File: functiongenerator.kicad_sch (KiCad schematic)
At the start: 47 parts, among them J1 Amplitude, J2 offset, J3 Amplitude, J4 offset, J5 Conn_01x02_Socket, U1 LM6172, U2 LM6172, X1 ?2271611-, X2 ?2271611-

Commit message: pre release v2
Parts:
- added TP1, TP2, TP3, TP4, TP5, TP6: TestPoint_Small, TestPoint:TestPoint_Pad_D1.0mm, symbol Connector:TestPoint_Small
- C1, C3, C5: footprint functiongenerator:E2,5-7 -> Capacitor_THT:CP_Radial_D12.5mm_P5.00mm
- C2, C4, C6, C7, C8, C9: footprint functiongenerator:C025-030X050 -> Capacitor_THT:C_Disc_D3.0mm_W1.6mm_P2.50mm
- DC1: footprint functiongenerator:SIP3 -> Converter_DCDC:Converter_DCDC_TRACO_TSR-1_THT; symbol functiongenerator-eagle-import:R-78C-1.0 -> TSR_1-2450:TSR_1-2450; Availability (none) -> In Stock; Check_prices (none) -> https://www.snapeda.com/parts/TSR%201-2450/Traco+Power/view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; Description_1 (none) -> 1 Amp POL switching regulator, wide input range, pos.-pos. 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; MANUFACTURER (none) -> Traco Power; MAXIMUM_PACKAGE_HEIGHT (none) -> 10.6mm; MF (none) -> Traco Power; MP (none) -> TSR 1-2450; PARTREV (none) -> Apr 27, 2020; Package (none) -> SIP-3 Traco Power; Price (none) -> None; STANDARD (none) -> Manufacturer Recommendations; SnapEDA_Link (none) -> https://www.snapeda.com/parts/TSR%201-2450/Traco+Power/view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
- J5: footprint Connector_PinHeader_2.54mm:PinHeader_1x02_P2.54mm_Vertical -> Connector_PinSocket_2.54mm:PinSocket_1x02_P2.54mm_Vertical
- SV1: renamed from SV2; footprint functiongenerator:FE07 -> Connector_PinSocket_2.54mm:PinSocket_1x07_P2.54mm_Vertical
- SV2: renamed from SV1; footprint functiongenerator:FE07 -> Connector_PinSocket_2.54mm:PinSocket_1x07_P2.54mm_Vertical
- SV4: footprint Connector_PinHeader_2.54mm:PinHeader_1x04_P2.54mm_Vertical -> Connector_PinSocket_2.54mm:PinSocket_1x04_P2.54mm_Vertical
- X1, X2: footprint functiongenerator:AMP_227161 -> Connector_Coaxial:LEMO-EPL.00.250.NTN
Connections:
- net at J3.1 (Pin_1), R6.2, U2.1: now also TP5.1
- net at R8.1, U2.7, X2.1: now also TP6.1
- net at R4.1, U1.7, X1.1: now also TP3.1
- net at J1.1 (Pin_1), R1.2, U1.1: now also TP2.1
- net at R13.1, SV2.1: now also TP4.1
- net at R10.1, SV1.1: now also TP1.1
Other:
- moved on the sheet: C3, D1, R9

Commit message: optimized pcb layout
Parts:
- C1: value ~ -> 470uF; symbol functiongenerator-eagle-import:CPOL-EUE2.5-7 -> Device:C_Polarized
- C10: renamed from C2; symbol functiongenerator-eagle-import:C-EU025-030X050 -> Device:C_Small
- C13: renamed from C6; symbol functiongenerator-eagle-import:C-EU025-030X050 -> Device:C_Small
- C14: renamed from C7; symbol functiongenerator-eagle-import:C-EU025-030X050 -> Device:C_Small
- C17: renamed from C3; value ~ -> 10uF; symbol functiongenerator-eagle-import:CPOL-EUE2.5-7 -> Device:C_Polarized
- C2: renamed from C5; value ~ -> 470uF; symbol functiongenerator-eagle-import:CPOL-EUE2.5-7 -> Device:C_Polarized
- C4: renamed from C8; symbol functiongenerator-eagle-import:C-EU025-030X050 -> Device:C_Small
- C5: renamed from C9; symbol functiongenerator-eagle-import:C-EU025-030X050 -> Device:C_Small
- C7: renamed from C16; value 2.2uF -> 10uF
- C8: renamed from C17; value 2.2uF -> 10uF
- C9: renamed from C4; symbol functiongenerator-eagle-import:C-EU025-030X050 -> Device:C_Small
- R1: renamed from R2; value 33 -> 330; footprint functiongenerator:0204_7 -> Resistor_THT:R_Axial_DIN0204_L3.6mm_D1.6mm_P7.62mm_Horizontal; symbol functiongenerator-eagle-import:R-EU_0204/7 -> Device:R
- R10: renamed from R4; footprint functiongenerator:0204_7 -> Resistor_THT:R_Axial_DIN0204_L3.6mm_D1.6mm_P7.62mm_Horizontal; symbol functiongenerator-eagle-import:R-EU_0204/7 -> Device:R
- R11: renamed from R7; footprint functiongenerator:0204_7 -> Resistor_THT:R_Axial_DIN0204_L3.6mm_D1.6mm_P7.62mm_Horizontal; symbol functiongenerator-eagle-import:R-EU_0204/7 -> Device:R
- R12: renamed from R8; footprint functiongenerator:0204_7 -> Resistor_THT:R_Axial_DIN0204_L3.6mm_D1.6mm_P7.62mm_Horizontal; symbol functiongenerator-eagle-import:R-EU_0204/7 -> Device:R
- R2: renamed from R3; value 33 -> 330; footprint functiongenerator:0204_7 -> Resistor_THT:R_Axial_DIN0204_L3.6mm_D1.6mm_P7.62mm_Horizontal; symbol functiongenerator-eagle-import:R-EU_0204/7 -> Device:R
- R7: renamed from R1; footprint functiongenerator:0204_7 -> Resistor_THT:R_Axial_DIN0204_L3.6mm_D1.6mm_P7.62mm_Horizontal; symbol functiongenerator-eagle-import:R-EU_0204/7 -> Device:R
- R8: renamed from R6; footprint functiongenerator:0204_7 -> Resistor_THT:R_Axial_DIN0204_L3.6mm_D1.6mm_P7.62mm_Horizontal; symbol functiongenerator-eagle-import:R-EU_0204/7 -> Device:R_Small
- R9: renamed from R5; footprint functiongenerator:0204_7 -> Resistor_THT:R_Axial_DIN0204_L3.6mm_D1.6mm_P7.62mm_Horizontal; symbol functiongenerator-eagle-import:R-EU_0204/7 -> Device:R
- RV1: value R_Potentiometer_Trim -> 2k
- SV1: renamed from SV3; symbol functiongenerator-eagle-import:MA03-1 -> Connector:Screw_Terminal_01x03
- SV3: renamed from SV1; value FE07-1 -> Conn_01x07_Socket; symbol functiongenerator-eagle-import:FE07-1 -> Connector:Conn_01x07_Socket
- SV4: renamed from SV2; symbol functiongenerator-eagle-import:FE07-1 -> Connector:Conn_01x07_Socket
- X1: value ?2271611- -> CON1; footprint Connector_Coaxial:LEMO-EPL.00.250.NTN -> BNC:LINX_CONBNC002; symbol functiongenerator-eagle-import:?2271611- -> CONBNC002:CONBNC002; Availability (none) -> In Stock; Check_prices (none) -> https://www.snapeda.com/parts/CONBNC002/TE+Connectivity/vie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; Description_1 (none) -> BNC Jack 50 Ohm PCB Through Hole; MF (none) -> TE Connectivity; MP (none) -> CONBNC002; Package (none) -> None; Price (none) -> None; Purchase-URL (none) -> https://www.snapeda.com/api/url_track_click_mouser/?unipart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; SnapEDA_Link (none) -> https://www.snapeda.com/parts/CONBNC002/TE+Connectivity/vie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
- X2: value ?2271611- -> CON2; footprint Connector_Coaxial:LEMO-EPL.00.250.NTN -> BNC:LINX_CONBNC002; symbol functiongenerator-eagle-import:?2271611- -> CONBNC002:CONBNC002; Availability (none) -> In Stock; Check_prices (none) -> https://www.snapeda.com/parts/CONBNC002/TE+Connectivity/vie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; Description_1 (none) -> BNC Jack 50 Ohm PCB Through Hole; MF (none) -> TE Connectivity; MP (none) -> CONBNC002; Package (none) -> None; Price (none) -> None; Purchase-URL (none) -> https://www.snapeda.com/api/url_track_click_mouser/?unipart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; SnapEDA_Link (none) -> https://www.snapeda.com/parts/CONBNC002/TE+Connectivity/vie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
- renumbered C12 to C11, C13 to C12, C14 to C15, C15 to C16, C10 to C3, C11 to C6, J5 to J1, J1 to J2, J2 to J4, J4 to J5, R9 to R13, R11 to R3, R10 to R4, R12 to R5, R13 to R6, SV4 to SV2, TP4 to TP2, TP2 to TP3, TP5 to TP4, TP3 to TP5
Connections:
- net +12v: now also C1.1; no longer C1.+
- net +5v: now also C17.1; no longer C17.+
- net -12v: now also C2.2; no longer C2.+
- net GND: now also C1.2, C17.2, C2.1, X1.S1, X1.S2, X2.S1, X2.S2; no longer C1.-, C17.-, C2.-
- net at J3.1 (Pin_1), TP4.1, U2.1: now also R8.1; no longer R8.2
- net at R12.2, U2.6 (-): now also R8.2; no longer R8.1
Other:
- moved on the sheet: J2, J3, J4, J5

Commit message: optimizing pcb design
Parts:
- R1, R11, R2, R9: footprint Resistor_THT:R_Axial_DIN0204_L3.6mm_D1.6mm_P7.62mm_Horizontal -> Resistor_THT:R_Axial_DIN0207_L6.3mm_D2.5mm_P7.62mm_Horizontal
- R10, R12, R7, R8: value 1000 -> 1k; footprint Resistor_THT:R_Axial_DIN0204_L3.6mm_D1.6mm_P7.62mm_Horizontal -> Resistor_THT:R_Axial_DIN0207_L6.3mm_D2.5mm_P7.62mm_Horizontal
- R13: value 390 -> 330
- R3, R4, R5, R6: footprint Resistor_THT:R_Axial_DIN0204_L3.6mm_D1.6mm_P5.08mm_Horizontal -> Resistor_THT:R_Axial_DIN0207_L6.3mm_D2.5mm_P7.62mm_Horizontal
- RV2: value R_Potentiometer_Trim -> 2k
- SV1: footprint TerminalBlock_Phoenix:TerminalBlock_Phoenix_PT-1,5-3-3.5-H_1x03_P3.50mm_Horizontal -> TerminalBlock_MetzConnect:TerminalBlock_MetzConnect_Type059_RT06303HBWC_1x03_P3.50mm_Horizontal
- SV4: value FE07-1 -> Conn_01x07_Socket
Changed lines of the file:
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@@
 			)
 		)
-		(property "Value" "1000"
+		(property "Value" "1k"
 			(at 160.782 127.508 90)
 			(effects
@@
 			)
 		)
-		(property "Footprint" "Resistor_THT:R_Axial_DIN0204_L3.6mm_D1.6mm_P7.62mm_Horizontal"
+		(property "Footprint" "Resistor_THT:R_Axial_DIN0207_L6.3mm_D2.5mm_P7.62mm_Horizontal"
 			(at 163.83 129.54 0)
 			(effects
@@
 			)
 		)
-		(property "Value" "R_Potentiometer_Trim"
+		(property "Value" "2k"
 			(at 113.7921 158.6921 0)
 			(effects
@@
 			)
 		)
-		(property "Footprint" "Resistor_THT:R_Axial_DIN0204_L3.6mm_D1.6mm_P7.62mm_Horizontal"
+		(property "Footprint" "Resistor_THT:R_Axial_DIN0207_L6.3mm_D2.5mm_P7.62mm_Horizontal"
 			(at 163.83 154.94 0)
 			(effects
@@
 			)
 		)
-		(property "Footprint" "Resistor_THT:R_Axial_DIN0204_L3.6mm_D1.6mm_P5.08mm_Horizontal"
+		(property "Footprint" "Resistor_THT:R_Axial_DIN0207_L6.3mm_D2.5mm_P7.62mm_Horizontal"
 			(at 119.38 114.808 90)
 			(effects
@@
 			)
 		)
-		(property "Value" "FE07-1"
+		(property "Value" "Conn_01x07_Socket"
 			(at 92.71 135.89 0)
 			(effects
@@
 				)
 				(justify left bottom)
-				(hide yes)
 			)
 		)
@@
 			)
 		)
-		(property "Footprint" "Resistor_THT:R_Axial_DIN0204_L3.6mm_D1.6mm_P5.08mm_Horizontal"
+		(property "Footprint" "Resistor_THT:R_Axial_DIN0207_L6.3mm_D2.5mm_P7.62mm_Horizontal"
 			(at 124.46 164.338 90)
 			(effects
@@
 			)
 		)
-		(property "Footprint" "Resistor_THT:R_Axial_DIN0204_L3.6mm_D1.6mm_P5.08mm_Horizontal"
+		(property "Footprint" "Resistor_THT:R_Axial_DIN0207_L6.3mm_D2.5mm_P7.62mm_Horizontal"
 			(at 119.38 118.618 90)
 			(effects
@@
 			)
 		)
-		(property "Value" "390"
+		(property "Value" "330"
 			(at 189.484 75.438 90)
 			(effects
@@
 			)
 		)
-		(property "Value" "1000"
+		(property "Value" "1k"
 			(at 149.606 117.094 90)
 			(effects
@@
 			)
 		)
-		(property "Footprint" "Resistor_THT:R_Axial_DIN0204_L3.6mm_D1.6mm_P7.62mm_Horizontal"
+		(property "Footprint" "Resistor_THT:R_Axial_DIN0207_L6.3mm_D2.5mm_P7.62mm_Horizontal"
 			(at 152.4 119.38 0)
 			(effects
@@
 			)
 		)
-		(property "Footprint" "Resistor_THT:R_Axial_DIN0204_L3.6mm_D1.6mm_P5.08mm_Horizontal"
+		(property "Footprint" "Resistor_THT:R_Axial_DIN0207_L6.3mm_D2.5mm_P7.62mm_Horizontal"
 			(at 124.46 160.528 90)
 			(effects
@@
 			)
 		)
-		(property "Footprint" "Resistor_THT:R_Axial_DIN0204_L3.6mm_D1.6mm_P7.62mm_Horizontal"
+		(property "Footprint" "Resistor_THT:R_Axial_DIN0207_L6.3mm_D2.5mm_P7.62mm_Horizontal"
 			(at 158.75 109.22 0)
 			(effects
@@
 			)
 		)
-		(property "Value" "1000"
+		(property "Value" "1k"
 			(at 165.354 172.72 90)
 			(effects
@@
 			)
 		)
-		(property "Footprint" "Resistor_THT:R_Axial_DIN0204_L3.6mm_D1.6mm_P7.62mm_Horizontal"
+		(property "Footprint" "Resistor_THT:R_Axial_DIN0207_L6.3mm_D2.5mm_P7.62mm_Horizontal"
 			(at 167.64 175.26 0)
 			(effects
@@
 			)
 		)
-		(property "Value" "1000"
+		(property "Value" "1k"
 			(at 160.02 167.132 90)
 			(effects
@@
 			)
 		)
-		(property "Footprint" "Resistor_THT:R_Axial_DIN0204_L3.6mm_D1.6mm_P7.62mm_Horizontal"
+		(property "Footprint" "Resistor_THT:R_Axial_DIN0207_L6.3mm_D2.5mm_P7.62mm_Horizontal"
 			(at 157.48 165.1 0)
 			(effects
@@
 			)
 		)
-		(property "Footprint" "TerminalBlock_Phoenix:TerminalBlock_Phoenix_PT-1,5-3-3.5-H_1x03_P3.50mm_Horizontal"
+		(property "Footprint" "TerminalBlock_MetzConnect:TerminalBlock_MetzConnect_Type059_RT06303HBWC_1x03_P3.50mm_Horizontal"
 			(at 76.2 71.12 0)
 			(effects
@@
 			)
 		)
-		(property "Footprint" "Resistor_THT:R_Axial_DIN0204_L3.6mm_D1.6mm_P7.62mm_Horizontal"
+		(property "Footprint" "Resistor_THT:R_Axial_DIN0207_L6.3mm_D2.5mm_P7.62mm_Horizontal"
 			(at 105.41 167.64 0)
 			(effects
@@
 			)
 		)
-		(property "Footprint" "Resistor_THT:R_Axial_DIN0204_L3.6mm_D1.6mm_P7.62mm_Horizontal"
+		(property "Footprint" "Resistor_THT:R_Axial_DIN0207_L6.3mm_D2.5mm_P7.62mm_Horizontal"
 			(at 102.87 129.54 0)
 			(effects

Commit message: optimizing pcb design
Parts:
- added R2, R4: 680, Resistor_THT:R_Axial_DIN0207_L6.3mm_D2.5mm_P7.62mm_Horizontal, symbol Device:R
- R11: renamed from R9; value 500 -> 520
- R13: renamed from R11; value 500 -> 520
- R5: renamed from R3; value 18k -> 10k
- R7: renamed from R5; value 18k -> 10k
- RV1, RV2: value 2k -> 500
- renumbered R8 to R10, R10 to R12, R12 to R14, R13 to R15, R2 to R3, R4 to R6, R6 to R8, R7 to R9
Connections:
- net -12v: now also R2.1, R4.1; no longer RV1.3, RV2.3
- new net: R4.2, RV2.3
- new net: R2.2, RV1.3
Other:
- moved on the sheet: RV1, RV2

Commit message: added gnd to inout connector to reduce grounding loops
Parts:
- SV2: value Conn_01x04_Socket -> Conn_01x05_Socket; footprint Connector_PinSocket_2.54mm:PinSocket_1x04_P2.54mm_Vertical -> Connector_PinSocket_2.54mm:PinSocket_1x05_P2.54mm_Vertical; symbol Connector:Conn_01x04_Socket -> Connector:Conn_01x05_Socket
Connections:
- net GND: now also SV2.5 (Pin_5)
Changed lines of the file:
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@@
+	(symbol
+		(lib_id "power:GND")
+		(at 81.28 109.22 90)
+		(unit 1)
+		(exclude_from_sim no)
+		(in_bom yes)
+		(on_board yes)
+		(dnp no)
+		(fields_autoplaced yes)
+		(property "Reference" "#PWR020"
+			(at 87.63 109.22 0)
+			(effects
+				(font
+					(size 1.27 1.27)
+				)
+				(hide yes)
+			)
+		)
+		(property "Value" "GND"
+			(at 84.455 109.22 90)
+			(effects
+				(font
+					(size 1.27 1.27)
+				)
+				(justify right)
+			)
+		)
+		(property "Footprint" ""
+			(at 81.28 109.22 0)
+			(effects
+				(font
+					(size 1.27 1.27)
+				)
+				(hide yes)
+			)
+		)
+		(property "Datasheet" ""
+			(at 81.28 109.22 0)
+			(effects
+				(font
+					(size 1.27 1.27)
+				)
+				(hide yes)
+			)
+		)
+		(property "Description" "Power symbol creates a global label with name \"GND\" , ground"
+			(at 81.28 109.22 0)
+			(effects
+				(font
+					(size 1.27 1.27)
+				)
+				(hide yes)
+			)
+		)
+		(pin "1"
+		)
+		(instances
+			(project "functiongenerator"
+				(path "/5565f228-82ce-48d9-9419-b221a0e0c70a"
+					(reference "#PWR020")
+					(unit 1)
+				)
+			)
+		)
+	)
 	(symbol
 		(lib_id "power:GND")
@@
 	)
 	(symbol
-		(lib_id "Connector:Conn_01x04_Socket")
-		(at 76.2 116.84 180)
+		(lib_id "Connector:Conn_01x05_Socket")
+		(at 76.2 114.3 180)
 		(unit 1)
 		(exclude_from_sim no)
@@
 		(dnp no)
 		(property "Reference" "SV2"
-			(at 78.994 120.904 0)
+			(at 78.994 118.364 0)
 			(effects
 				(font
@@
 			)
 		)
-		(property "Value" "Conn_01x04_Socket"
-			(at 76.2 109.22 0)
-			(effects
-				(font
-					(size 1.27 1.27)
-				)
-				(hide yes)
-			)
-		)
-		(property "Footprint" "Connector_PinSocket_2.54mm:PinSocket_1x04_P2.54mm_Vertical"
-			(at 76.2 116.84 0)
+		(property "Value" "Conn_01x05_Socket"
+			(at 76.2 106.68 0)
+			(effects
+				(font
+					(size 1.27 1.27)
+				)
+				(hide yes)
+			)
+		)
+		(property "Footprint" "Connector_PinSocket_2.54mm:PinSocket_1x05_P2.54mm_Vertical"
+			(at 76.2 114.3 0)
 			(effects
 				(font
@@
 		)
 		(property "Datasheet" "~"
-			(at 76.2 116.84 0)
+			(at 76.2 114.3 0)
 			(effects
 				(font
@@
 		)
 		(property "Description" "Generic connector, single row, 01x04, script generated"
-			(at 76.2 116.84 0)
+			(at 76.2 114.3 0)
 			(effects
 				(font
@@
 		(pin "4"
 		)
-		(instances
+		(pin "5"
+		)
+		(instances

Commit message: attached agnd to common gnd moved +5v connector to board edge
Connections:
- net GND: now also SV3.2 (Pin_2), SV4.2 (Pin_2)
- no-connect marks 2 -> 0
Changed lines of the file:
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@@
+	)
+	(junction
+		(at 96.52 143.51)
+		(diameter 0)
+		(color 0 0 0 0)
 	)
 	(junction
@@
 	)
 	(junction
+		(at 96.52 109.22)
+		(diameter 0)
+		(color 0 0 0 0)
+	)
+	(junction
 		(at 105.41 148.59)
 		(diameter 0)
@@
 		(color 0 0 0 0)
 	)
-	(no_connect
-		(at 96.52 153.67)
-	)
-	(no_connect
-		(at 96.52 119.38)
-	)
 	(wire
 		(pts
@@
 	(wire
 		(pts
+			(xy 96.52 119.38) (xy 99.06 119.38)
+		)
+		(stroke
+			(width 0)
+			(type default)
+		)
+	)
+	(wire
+		(pts
 			(xy 106.68 116.84) (xy 106.68 121.92)
 		)
@@
 	(wire
 		(pts
+			(xy 97.79 144.78) (xy 96.52 144.78)
+		)
+		(stroke
+			(width 0)
+			(type default)
+		)
+	)
+	(wire
+		(pts
 			(xy 105.41 140.97) (xy 105.41 143.51)
 		)
@@
 	(wire
 		(pts
+			(xy 96.52 110.49) (xy 99.06 110.49)
+		)
+		(stroke
+			(width 0)
+			(type default)
+		)
+	)
+	(wire
+		(pts
+			(xy 99.06 110.49) (xy 99.06 119.38)
+		)
+		(stroke
+			(width 0)
+			(type default)
+		)
+	)
+	(wire
+		(pts
 			(xy 115.57 109.22) (xy 115.57 113.03)
 		)
@@
 	(wire
 		(pts
+			(xy 96.52 153.67) (xy 97.79 153.67)
+		)
+		(stroke
+			(width 0)
+			(type default)
+		)
+	)
+	(wire
+		(pts
 			(xy 143.51 156.21) (xy 144.78 156.21)
 		)
@@
 	(wire
 		(pts
+			(xy 96.52 109.22) (xy 96.52 110.49)
+		)
+		(stroke
+			(width 0)
+			(type default)
+		)
+	)
+	(wire
+		(pts
 			(xy 105.41 99.06) (xy 105.41 101.6)
 		)
@@
 	(wire
 		(pts
+			(xy 96.52 143.51) (xy 96.52 144.78)
+		)
+		(stroke
+			(width 0)
+			(type default)
+		)
+	)
+	(wire
+		(pts
 			(xy 81.28 116.84) (xy 96.52 116.84)
 		)
@@
 		)
 		(stroke
+			(width 0)
+			(type default)
+		)
+	)
+	(wire
+		(pts
+			(xy 97.79 153.67) (xy 97.79 144.78)
+		)
+		(stroke

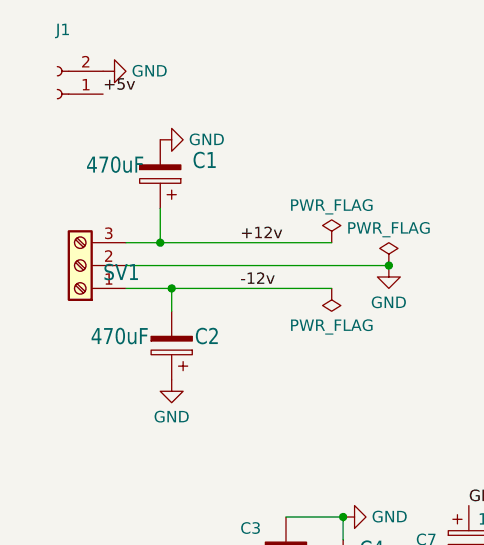
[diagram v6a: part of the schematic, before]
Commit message: seperated channels more updated label to v1.1
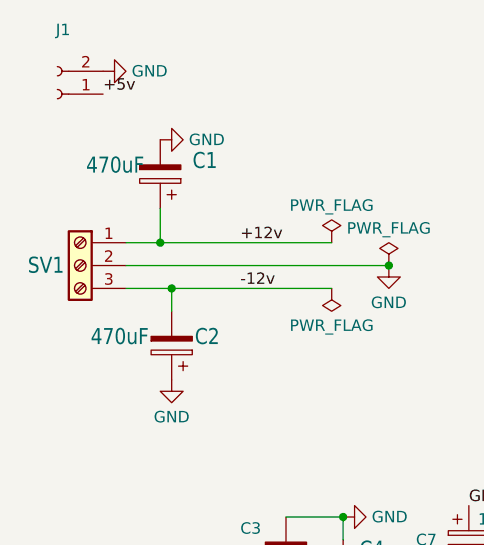
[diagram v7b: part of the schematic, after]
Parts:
- J2, J3: footprint Connector_JST:JST_XH_B2B-XH-AM_1x02_P2.50mm_Vertical -> Connector_JST:JST_XH_B2B-XH-A_1x02_P2.50mm_Vertical
- J4, J5: footprint Connector_JST:JST_XH_B3B-XH-AM_1x03_P2.50mm_Vertical -> Connector_JST:JST_XH_B3B-XH-A_1x03_P2.50mm_Vertical
- SV1: footprint TerminalBlock_MetzConnect:TerminalBlock_MetzConnect_Type059_RT06303HBWC_1x03_P3.50mm_Horizontal -> TerminalBlock_Phoenix:TerminalBlock_Phoenix_PT-1,5-3-3.5-H_1x03_P3.50mm_Horizontal
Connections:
- net +12v: now also SV1.1 (Pin_1); no longer SV1.3 (Pin_3)
- net -12v: now also SV1.3 (Pin_3); no longer SV1.1 (Pin_1)
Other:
- moved on the sheet: SV1
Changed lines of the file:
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@@
 			)
 		)
-		(property "Footprint" "Connector_JST:JST_XH_B2B-XH-AM_1x02_P2.50mm_Vertical"
+		(property "Footprint" "Connector_JST:JST_XH_B2B-XH-A_1x02_P2.50mm_Vertical"
 			(at 115.57 182.88 0)
 			(effects
@@
 			)
 		)
-		(property "Footprint" "Connector_JST:JST_XH_B3B-XH-AM_1x03_P2.50mm_Vertical"
+		(property "Footprint" "Connector_JST:JST_XH_B3B-XH-A_1x03_P2.50mm_Vertical"
 			(at 147.32 100.33 0)
 			(effects
@@
 			)
 		)
-		(property "Footprint" "Connector_JST:JST_XH_B2B-XH-AM_1x02_P2.50mm_Vertical"
+		(property "Footprint" "Connector_JST:JST_XH_B2B-XH-A_1x02_P2.50mm_Vertical"
 			(at 105.41 138.43 0)
 			(effects
@@
 			)
 		)
-		(property "Footprint" "Connector_JST:JST_XH_B3B-XH-AM_1x03_P2.50mm_Vertical"
+		(property "Footprint" "Connector_JST:JST_XH_B3B-XH-A_1x03_P2.50mm_Vertical"
 			(at 152.4 147.32 0)
 			(effects
@@
 	(symbol
 		(lib_id "Connector:Screw_Terminal_01x03")
-		(at 76.2 71.12 180)
+		(at 76.2 71.12 0)
+		(mirror y)
 		(unit 1)
 		(exclude_from_sim no)
@@
 		(dnp no)
 		(property "Reference" "SV1"
-			(at 82.804 70.866 0)
+			(at 74.422 72.136 0)
 			(effects
 				(font
@@
 		)
 		(property "Value" "TERM-3"
-			(at 77.47 63.5 0)
+			(at 77.47 78.74 0)
 			(effects
 				(font
@@
 			)
 		)
-		(property "Footprint" "TerminalBlock_MetzConnect:TerminalBlock_MetzConnect_Type059_RT06303HBWC_1x03_P3.50mm_Horizontal"
+		(property "Footprint" "TerminalBlock_Phoenix:TerminalBlock_Phoenix_PT-1,5-3-3.5-H_1x03_P3.50mm_Horizontal"
 			(at 76.2 71.12 0)
 			(effects
